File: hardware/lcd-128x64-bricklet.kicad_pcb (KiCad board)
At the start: 2 copper layers, 85 x 55 mm, 45 parts, among them P1 CON-SENSOR2, P2 Debug, P3 BOOT, P4 CON_4Wire_ER-TP028-1, Q1 2N7002, U1 XMC130024, U2 TSC2046E, U3 LCD-ERC12864, U4 DRILL, U5 DRILL, U6 DRILL, U7 DRILL

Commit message: Minor layout adjustments
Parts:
- moved G*** 6.34 mm to (103.1, 90.4), turned to 90 degrees
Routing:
- net VCC: track 171.3 -> 133.0 mm
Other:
- board text added: "LCD 128x64 1.0"
- board text removed: "1.0"
- board text removed: "LCD 128x64"
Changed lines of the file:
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@@
     (area 96.709499 61.109499 182.090501 116.490501)
     (thickness 1.6)
-    (drawings 17)
+    (drawings 16)
     (tracks 512)
     (zones 0)
@@
   )
   (setup
-    (last_trace_width 0.3)
+    (last_trace_width 0.55)
     (user_trace_width 0.2)
     (user_trace_width 0.25)
@@
   )
   (module kicad-libraries:Logo_31x31 (layer B.Cu)
-    (at 102.4 96.7 180)
-    (fp_text reference G*** (at 1.34874 -2.97434 180) (layer B.SilkS) hide
+    (at 103.1 90.4 90)
+    (fp_text reference G*** (at 1.34874 -2.97434 90) (layer B.SilkS) hide
       (effects (font (size 0.29972 0.29972) (thickness 0.0762)) (justify mirror))
     )
-    (fp_text value Logo_31x31 (at 1.651 -0.59944 180) (layer B.SilkS) hide
+    (fp_text value Logo_31x31 (at 1.651 -0.59944 90) (layer B.SilkS) hide
       (effects (font (size 0.29972 0.29972) (thickness 0.0762)) (justify mirror))
     )
@@
     )
   )
-  (gr_text "1.0\n" (at 100.8 102.8) (layer B.SilkS)
-    (effects (font (size 0.6 0.6) (thickness 0.15)) (justify mirror))
-  )
   (gr_line (start 168.5 61.3) (end 179.4 61.3) (angle 90) (layer Edge.Cuts) (width 0.381))
   (gr_line (start 167.5 62.3) (end 168.5 61.3) (angle 90) (layer Edge.Cuts) (width 0.381))
@@
     (effects (font (size 0.8 0.8) (thickness 0.15)))
   )
-  (gr_text "LCD 128x64" (at 100.8 101.7) (layer B.SilkS)
-    (effects (font (size 0.6 0.6) (thickness 0.15)) (justify mirror))
+  (gr_text "LCD 128x64\n1.0\n" (at 179.7 88.8 270) (layer B.SilkS)
+    (effects (font (size 0.8 0.8) (thickness 0.15)) (justify mirror))
   )
-  (gr_text tinkerforge.com (at 100.8 100.5) (layer B.SilkS)
-    (effects (font (size 0.6 0.6) (thickness 0.15)) (justify mirror))
+  (gr_text tinkerforge.com (at 99 88.8 270) (layer B.SilkS)
+    (effects (font (size 0.8 0.8) (thickness 0.15)) (justify mirror))
   )
   (gr_text Status (at 180.5 75.7 90) (layer F.SilkS)
@@
   (segment (start 175.86 85.2) (end 175.3 85.2) (width 0.25) (layer F.Cu) (net 2))
   (segment (start 176.01 85.05) (end 175.86 85.2) (width 0.25) (layer F.Cu) (net 2))
+  (segment (start 173.7 89.95) (end 172.45 89.95) (width 0.55) (layer F.Cu) (net 3))
+  (segment (start 168.6 78.3) (end 168.6 77.34) (width 0.55) (layer F.Cu) (net 3))
+  (segment (start 169.7 79.4) (end 168.6 78.3) (width 0.55) (layer F.Cu) (net 3))
+  (segment (start 169.7 87.2) (end 169.7 79.4) (width 0.55) (layer F.Cu) (net 3))
+  (segment (start 172.45 89.95) (end 169.7 87.2) (width 0.55) (layer F.Cu) (net 3))
+  (segment (start 177.3 90.05) (end 178.45 90.05) (width 0.25) (layer F.Cu) (net 3))
+  (segment (start 179 89.5) (end 179 80.5501) (width 0.25) (layer F.Cu) (net 3))
+  (segment (start 178.45 90.05) (end 179 89.5) (width 0.25) (layer F.Cu) (net 3))
   (segment (start 161.62566 107.02306) (end 158.58306 107.02306) (width 0.3) (layer F.Cu) (net 3))
   (segment (start 158.48 106.92) (end 158.48 106.93) (width 0.3) (layer F.Cu) (net 3))
   (segment (start 158.58306 107.02306) (end 158.48 106.92) (width 0.3) (layer F.Cu) (net 3))
-  (segment (start 179 80.5501) (end 180.5 80.5501) (width 0.3) (layer F.Cu) (net 3))
-  (segment (start 165.80076 108.9) (end 171.67 108.9) (width 0.3) (layer F.Cu) (net 3))
-  (segment (start 179 101.57) (end 179 80.5501) (width 0.3) (layer F.Cu) (net 3))
-  (segment (start 171.67 108.9) (end 179 101.57) (width 0.3) (layer F.Cu) (net 3))
+  (segment (start 179 80.5501) (end 180.5 80.5501) (width 0.25) (layer F.Cu) (net 3))
   (segment (start 159.7 103.65) (end 158.66 103.65) (width 0.55) (layer F.Cu) (net 3))
   (segment (start 165.80076 109.99924) (end 165.80076 108.9) (width 0.55) (layer F.Cu) (net 3))
@@
   (segment (start 171.69 90.684998) (end 169.39 92.984998) (width 0.55) (layer F.Cu) (net 3))
   (segment (start 171.69 90.68) (end 171.69 90.684998) (width 0.55) (layer F.Cu) (net 3))
-  (segment (start 169.95 77.34) (end 169.95 77.94) (width 0.55) (layer F.Cu) (net 3))
-  (segment (start 169.79 87.27) (end 172.445 89.925) (width 0.55) (layer F.Cu) (net 3))
   (segment (start 172.445 89.925) (end 172.47 89.95) (width 0.55) (layer F.Cu) (net 3))
-  (segment (start 169.79 78.1) (end 169.79 87.27) (width 0.55) (layer F.Cu) (net 3))
-  (segment (start 169.95 77.94) (end 169.79 78.1) (width 0.55) (layer F.Cu) (net 3))
   (segment (start 172.47 89.95) (end 173.7 89.95) (width 0.55) (layer F.Cu) (net 3))
   (segment (start 137.03076 71.54) (end 137.03076 70.96076) (width 0.55) (layer F.Cu) (net 3))
@@
   (segment (start 136.57 68.81) (end 136.57 70.02) (width 0.55) (layer F.Cu) (net 3))
   (segment (start 136.225 68.465) (end 136.57 68.81) (width 0.55) (layer F.Cu) (net 3))
-  (segment (start 169.95 77.34) (end 161.44 77.34) (width 0.55) (layer F.Cu) (net 3))
-  (segment (start 161.44 77.34) (end 158.09 73.99) (width 0.55) (layer F.Cu) (net 3))
-  (segment (start 158.09 73.99) (end 157.44 73.99) (width 0.55) (layer F.Cu) (net 3))
-  (segment (start 157.44 73.99) (end 156.86 73.41) (width 0.55) (layer F.Cu) (net 3))
-  (segment (start 156.86 73.41) (end 156.86 70.94) (width 0.55) (layer F.Cu) (net 3))
-  (segment (start 156.86 70.94) (end 156.45 70.53) (width 0.55) (layer F.Cu) (net 3))
-  (segment (start 156.45 70.53) (end 140.01 70.53) (width 0.55) (layer F.Cu) (net 3))
-  (segment (start 140.01 70.53) (end 138.87 71.67) (width 0.55) (layer F.Cu) (net 3))
+  (segment (start 169.95 77.34) (end 168.6 77.34) (width 0.55) (layer F.Cu) (net 3))
+  (segment (start 168.6 77.34) (end 161.44 77.34) (width 0.55) (layer F.Cu) (net 3))
   (segment (start 138.87 71.67) (end 137.08 71.67) (width 0.55) (layer F.Cu) (net 3))
+  (segment (start 140.01 70.53) (end 138.87 71.67) (width 0.55) (layer F.Cu) (net 3))
+  (segment (start 156.45 70.53) (end 140.01 70.53) (width 0.55) (layer F.Cu) (net 3))
+  (segment (start 156.86 70.94) (end 156.45 70.53) (width 0.55) (layer F.Cu) (net 3))
+  (segment (start 156.86 73.41) (end 156.86 70.94) (width 0.55) (layer F.Cu) (net 3))
+  (segment (start 157.44 73.99) (end 156.86 73.41) (width 0.55) (layer F.Cu) (net 3))
+  (segment (start 158.09 73.99) (end 157.44 73.99) (width 0.55) (layer F.Cu) (net 3))
+  (segment (start 161.44 77.34) (end 158.09 73.99) (width 0.55) (layer F.Cu) (net 3))
   (segment (start 173.7 89.95) (end 172.47 89.95) (width 0.3) (layer F.Cu) (net 3))
-  (segment (start 169.89 87.37) (end 169.89 77.4) (width 0.3) (layer F.Cu) (net 3))
-  (segment (start 172.47 89.95) (end 169.89 87.37) (width 0.3) (layer F.Cu) (net 3))
   (segment (start 169.89 77.4) (end 169.95 77.34) (width 0.3) (layer F.Cu) (net 3))
   (segment (start 122.47 70.01) (end 123.97 70.01) (width 0.55) (layer F.Cu) (net 3))
@@
   (segment (start 133.685 63.65) (end 133.685 69.995) (width 0.55) (layer F.Cu) (net 8))
   (segment (start 133.685 69.995) (end 133.61 70.07) (width 0.55) (layer F.Cu) (net 8))
-  (segment (start 180.5 78.8499) (end 180.5 72.75) (width 0.2) (layer F.Cu) (net 9))
+  (segment (start 180.5 78.8499) (end 180.5 72.75) (width 0.25) (layer F.Cu) (net 9))
   (segment (start 175.375 87.6493) (end 175.7493 87.6493) (width 0.25) (layer F.Cu) (net 10))
   (segment (start 176.33 88.8) (end 177.3 88.8) (width 0.25) (layer F.Cu) (net 10))
@@
   (segment (start 138.29 64.96) (end 137.495 64.165) (width 0.2) (layer F.Cu) (net 41))
   (segment (start 137.495 64.165) (end 137.495 63.65) (width 0.2) (layer F.Cu) (net 41))
-  (segment (start 179 78.8499) (end 179 72.76) (width 0.2) (layer F.Cu) (net 42))
+  (segment (start 179 78.8499) (end 179 72.76) (width 0.25) (layer F.Cu) (net 42))
   (segment (start 179 72.76) (end 179.01 72.75) (width 0.2) (layer F.Cu) (net 42))
   (segment (start 174.25 75.375) (end 174.25 74.47) (width 0.2) (layer F.Cu) (net 43))

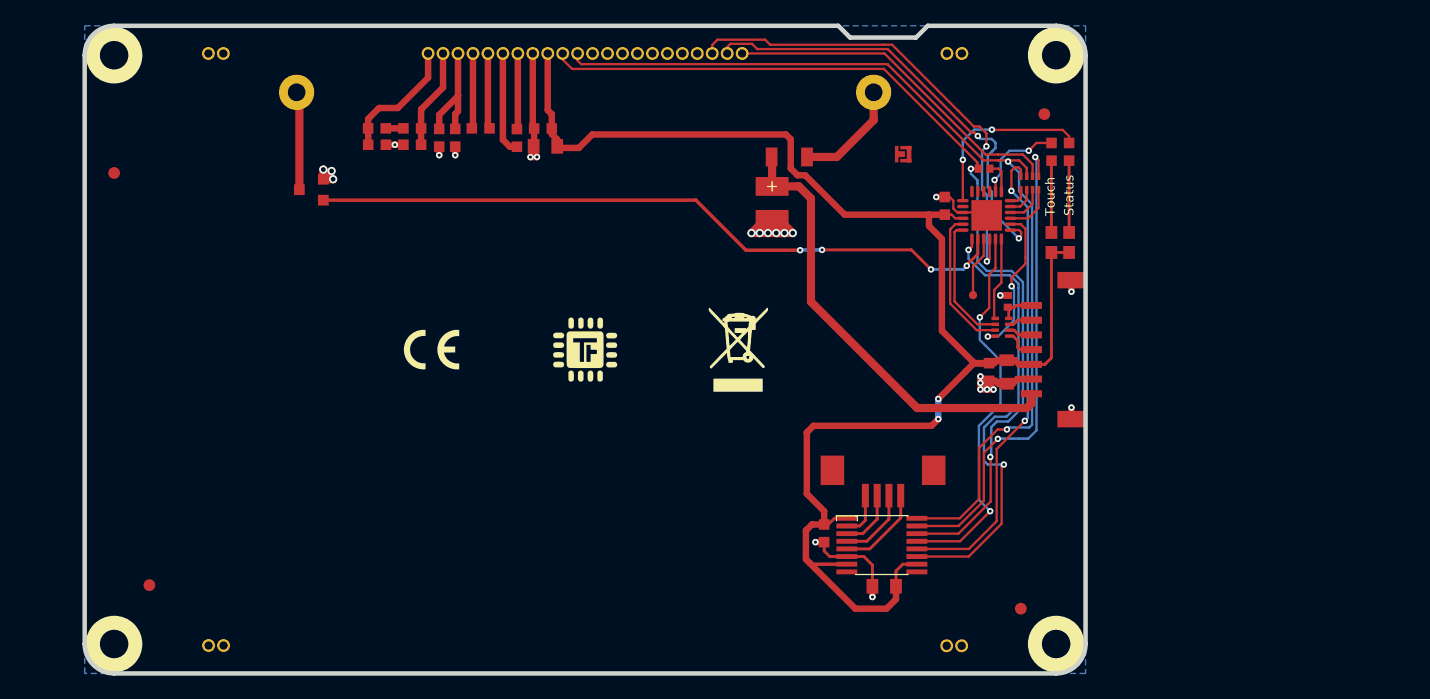
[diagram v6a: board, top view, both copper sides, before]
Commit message: hardware changes
 * move touchscreen connector +2mm
 * remove unneccssary resistors
 * move led positions and texts
 * swap led connections
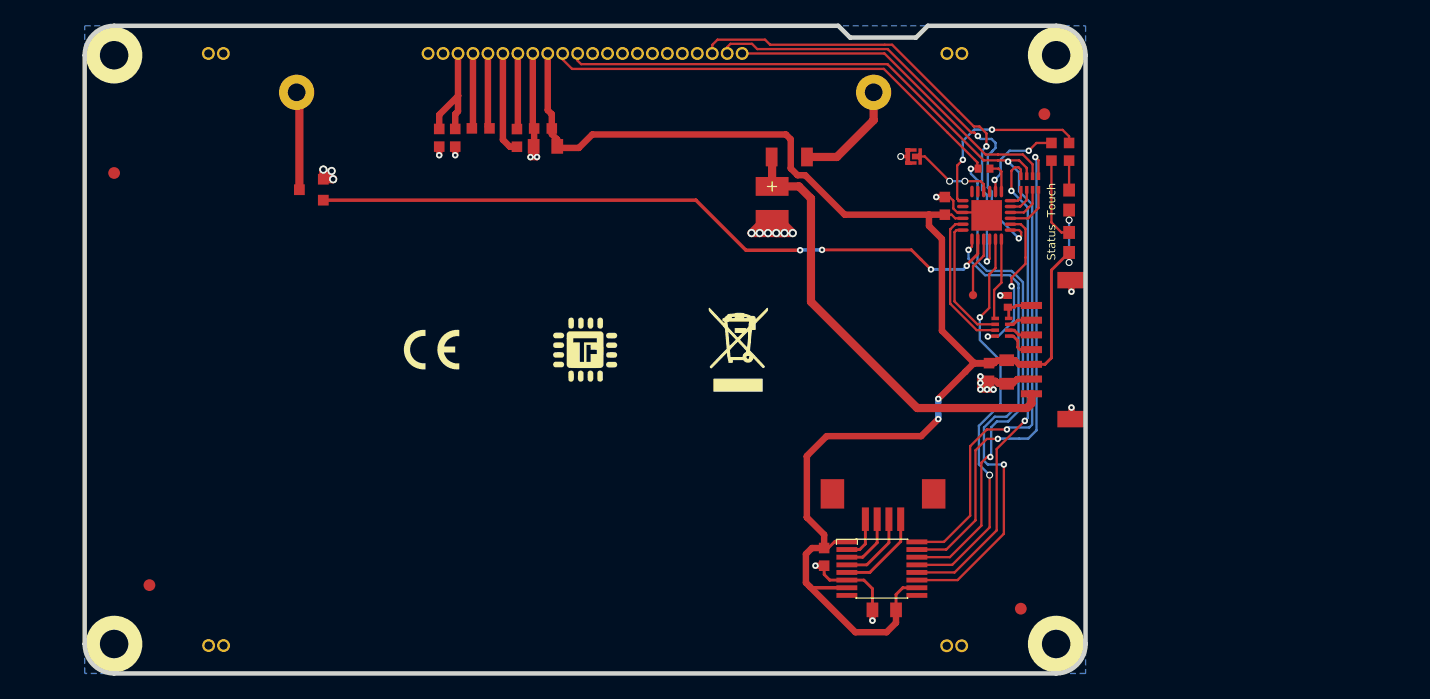
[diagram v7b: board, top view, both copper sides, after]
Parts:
- removed R2, R4: DNP, kicad-libraries:R0603F
- removed R3, R5: 0, kicad-libraries:R0603F
- moved D2 3.90 mm to (180.5, 76.1)
- moved C5 2.00 mm to (164.8, 110.9)
- moved C6 2.00 mm to (159.7, 106.4)
- moved P4 2.00 mm to (164.7, 103.2)
- moved U2 2.00 mm to (164.6, 107.4)
- moved R1 1.50 mm to (179.0, 72.0)
- moved R8 1.49 mm to (180.5, 72.0)
- moved P3 0.91 mm to (167.3, 72.4), turned to 0 degrees
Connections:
- U1 pad 2: Net-(R8-Pad1) -> Net-(R1-Pad1)
- U1 pad 3: Net-(U1-Pad3) -> (no net)
- U1 pad 5: Net-(U1-Pad5) -> (no net)
- U1 pad 6: Net-(U1-Pad6) -> (no net)
- U1 pad 7: Net-(R1-Pad1) -> Net-(R8-Pad1)
- U1 pad 8: Net-(U1-Pad8) -> (no net)
- U2 pad 8: Net-(U2-Pad8) -> (no net)
- U2 pad 9: Net-(U2-Pad9) -> (no net)
- U3 pad 21: Net-(R4-Pad2) -> GND
- U3 pad 22: Net-(R2-Pad2) -> GND
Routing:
- net Net-(R2-Pad2): track 11.0 -> 0.00 mm
- net Net-(R4-Pad2): track 8.52 -> 0.00 mm
- net Net-(R8-Pad1): track 7.87 -> 16.0 mm
- net Net-(R1-Pad1): track 15.3 -> 7.87 mm
- net Net-(P3-Pad2): track 0.00 -> 7.40 mm, vias 0 -> 2
- net VCC: track 133.0 -> 136.7 mm, vias 2 -> 4
- net Net-(D2-Pad2): track 6.10 -> 2.50 mm
- net M-CS-TS: track 40.9 -> 42.9 mm
- net M-CLK: track 82.2 -> 83.9 mm
- net M-MOSI: track 81.0 -> 82.7 mm
- net TS-BUSY: track 32.8 -> 34.4 mm
- net PENIRQ: track 39.0 -> 40.4 mm
- net M-MISO: track 40.7 -> 42.0 mm
- net Net-(D1-Pad2): track 6.10 -> 7.10 mm
- net GND: track 60.6 -> 61.4 mm
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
